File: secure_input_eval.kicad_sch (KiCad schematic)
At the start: 64 parts, among them CON1_STLINK1 ST-LINK, J10 masa pomiarowa, J18_CPU_CON1 Conn_CPU, J19 masa pomiarowa, J23 masa pomiarowa, J24 masa pomiarowa, J25 masa pomiarowa, J26 masa pomiarowa, J27_USART3 USART, J28_PIN14_PA7 TOUCH_SINGLE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

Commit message: TITLES&SUBTITLES POSITIONS & NAMES.
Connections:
- net SW5_TCH: now also J18_CPU_CON1.14 (Pin_14)
- net SW7_touch_single: no longer J18_CPU_CON1.14 (Pin_14)

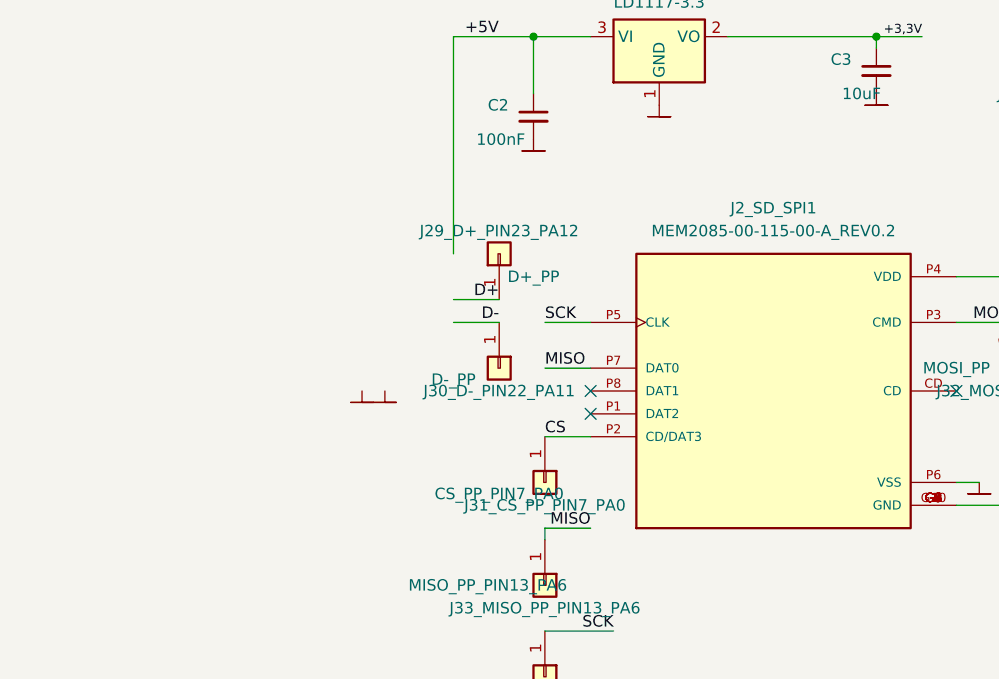
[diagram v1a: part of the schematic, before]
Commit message: symbole i footprinty #1
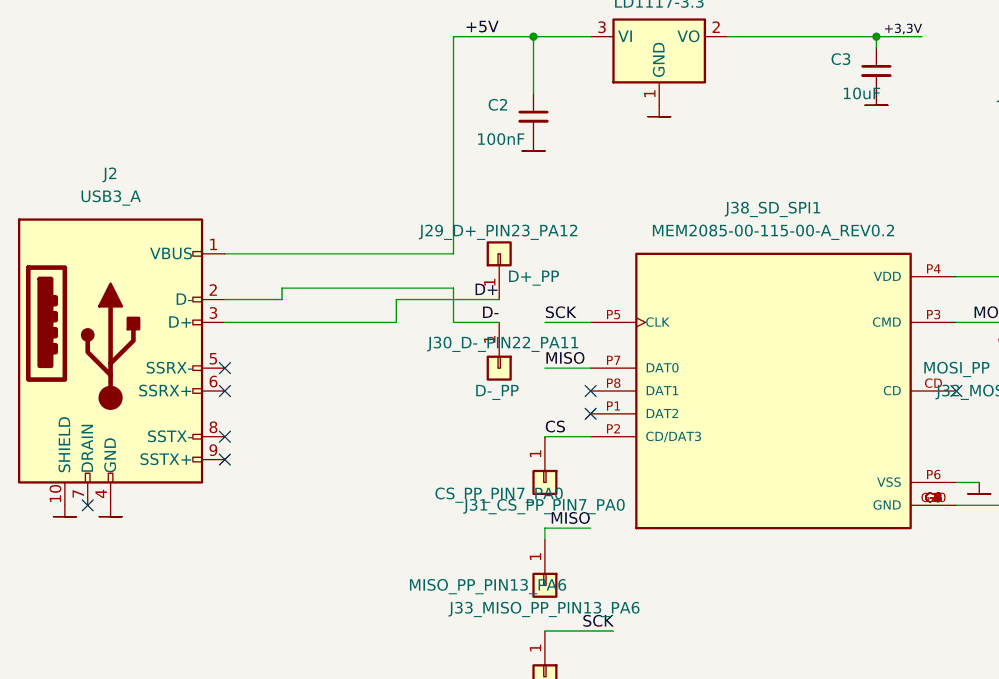
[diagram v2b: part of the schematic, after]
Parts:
- added J2: USB3_A, foots6:USB3_A_Amphenol_GSB316441CEU, symbol Connector:USB3_A
- H5: footprint secure_input_pen:MountingHole_2mm -> foots6:MountingHole_2mm
- renumbered J2_SD_SPI1 to J38_SD_SPI1
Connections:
- net +5V: now also J2.1 (VBUS)
- net D+: now also J2.3 (D+)
- net D-: now also J2.2 (D-)
- net masa: now also J2.10 (SHIELD), J2.4 (GND)
- no-connect marks 3 -> 8
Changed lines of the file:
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@@
 	)
 	(no_connect
+		(at -8.89 74.93)
+	)
+	(no_connect
 		(at 87.63 62.23)
 	)
 	(no_connect
+		(at 6.35 69.85)
+	)
+	(no_connect
+		(at 6.35 59.69)
+	)
+	(no_connect
+		(at 6.35 62.23)
+	)
+	(no_connect
 		(at 46.99 62.23)
 	)
 	(no_connect
+		(at 6.35 67.31)
+	)
+	(no_connect
 		(at 46.99 64.77)
 	)
 	(wire
 		(pts
+			(xy 12.7 52.07) (xy 6.35 52.07)
+		)
+		(stroke
+			(width 0)
+			(type default)
+		)
+	)
+	(wire
+		(pts
 			(xy 204.47 127) (xy 209.55 127)
 		)
@@
 	(wire
 		(pts
+			(xy 6.35 46.99) (xy 31.75 46.99)
+		)
+		(stroke
+			(width 0)
+			(type default)
+		)
+	)
+	(wire
+		(pts
 			(xy 262.89 130.302) (xy 270.002 130.302)
 		)
@@
 	(wire
 		(pts
+			(xy 31.75 50.8) (xy 12.7 50.8)
+		)
+		(stroke
+			(width 0)
+			(type default)
+		)
+	)
+	(wire
+		(pts
 			(xy 156.972 111.76) (xy 168.91 111.76)
 		)
@@
 	(wire
 		(pts
+			(xy 25.4 52.07) (xy 36.83 52.07)
+		)
+		(stroke
+			(width 0)
+			(type default)
+		)
+	)
+	(wire
+		(pts
 			(xy 140.97 52.07) (xy 149.86 52.07)
 		)
@@
 	(wire
 		(pts
-			(xy 163.83 129.54) (xy 168.91 129.54)
+			(xy 12.7 50.8) (xy 12.7 52.07)
 		)
 		(stroke
@@
 	(wire
 		(pts
-			(xy 241.3 139.7) (xy 247.65 139.7)
+			(xy 163.83 129.54) (xy 168.91 129.54)
 		)
 		(stroke
@@
 	(wire
 		(pts
-			(xy 118.11 95.25) (xy 113.03 95.25)
+			(xy 241.3 139.7) (xy 247.65 139.7)
 		)
 		(stroke
@@
 	(wire
 		(pts
-			(xy 31.75 52.07) (xy 36.83 52.07)
+			(xy 118.11 95.25) (xy 113.03 95.25)
 		)
 		(stroke
@@
 	(wire
 		(pts
+			(xy 31.75 54.61) (xy 31.75 50.8)
+		)
+		(stroke
+			(width 0)
+			(type default)
+		)
+	)
+	(wire
+		(pts
 			(xy 161.29 41.91) (xy 163.83 41.91)
 		)
@@
 	(wire
 		(pts
+			(xy 6.35 54.61) (xy 25.4 54.61)
+		)
+		(stroke
+			(width 0)
+			(type default)
+		)
+	)
+	(wire
+		(pts
 			(xy 204.47 124.46) (xy 209.55 124.46)
 		)
@@
 	(wire
 		(pts
+			(xy 25.4 54.61) (xy 25.4 52.07)
+		)
+		(stroke
+			(width 0)
+			(type default)
+		)
+	)
+	(wire
+		(pts
 			(xy 87.63 54.61) (xy 93.98 54.61)
 		)
@@
 			)
 		)
-		(property "Footprint" "secure_input_pen:MountingHole_2mm"
+		(property "Footprint" "foots6:MountingHole_2mm"
 			(at 208.28 17.78 0)
 			(effects
@@
 		(dnp no)
 		(fields_autoplaced yes)
-		(property "Reference" "J2_SD_SPI1"
+		(property "Reference" "J38_SD_SPI1"
 			(at 67.31 41.91 0)
 			(effects
@@
 			(project ""
 				(path "/df5b5a44-5c39-424a-a3aa-4eb40edf4ed4"
-					(reference "J2_SD_SPI1")
+					(reference "J38_SD_SPI1")
 					(unit 1)
 				)
@@
 	(symbol
 		(lib_id "sp3jdz:masa")
-		(at 24.13 62.23 0)
+		(at -11.43 74.93 0)
 		(unit 1)
 		(exclude_from_sim no)
@@
 		(fields_autoplaced yes)
 		(property "Reference" "#PWR04"
-			(at 24.13 68.58 0)
+			(at -11.43 81.28 0)
 			(effects
 				(font
@@
 		)
 		(property "Value" "masa"
-			(at 24.13 64.77 0)
+			(at -11.43 77.47 0)
 			(effects
 				(font
@@
 		)
 		(property "Footprint" ""
-			(at 24.13 62.23 0)
+			(at -11.43 74.93 0)
 			(effects
 				(font
@@
 		)
 		(property "Datasheet" ""
-			(at 24.13 62.23 0)
+			(at -11.43 74.93 0)
 			(effects
 				(font
@@
 		)
 		(property "Description" ""
-			(at 24.13 62.23 0)
+			(at -11.43 74.93 0)
 			(effects
 				(font
@@
 	)
 	(symbol
+		(lib_id "Connector:USB3_A")
+		(at -6.35 57.15 0)
+		(unit 1)
+		(exclude_from_sim no)
+		(in_bom yes)
+		(on_board yes)
+		(dnp no)
+		(fields_autoplaced yes)
+		(property "Reference" "J2"
+			(at -6.35 38.1 0)
+			(effects
+				(font
+					(size 1.27 1.27)
+				)
+			)
+		)
+		(property "Value" "USB3_A"
+			(at -6.35 40.64 0)
+			(effects
+				(font
+					(size 1.27 1.27)
+				)
+			)
+		)
+		(property "Footprint" "foots6:USB3_A_Amphenol_GSB316441CEU"
+			(at -2.54 54.61 0)
+			(effects
+				(font
+					(size 1.27 1.27)
+				)
+				(hide yes)
+			)
+		)
+		(property "Datasheet" "~"
+			(at -2.54 54.61 0)
+			(effects
+				(font
+					(size 1.27 1.27)
+				)
+				(hide yes)
+			)
+		)
+		(property "Description" "USB 3.0 A connector"
+			(at -6.35 57.15 0)
+			(effects
+				(font
+					(size 1.27 1.27)
+				)
+				(hide yes)
+			)
+		)
+		(pin "1"
+		)
+		(pin "10"
+		)
+		(pin "7"
+		)
+		(pin "4"
+		)
+		(pin "3"
+		)
+		(pin "6"
+		)
+		(pin "5"
+		)
+		(pin "9"
+		)
+		(pin "2"
+		)
+		(pin "8"
+		)
+		(instances
+			(project ""
+				(path "/df5b5a44-5c39-424a-a3aa-4eb40edf4ed4"
+					(reference "J2")
+					(unit 1)
+				)
+			)
+		)
+	)
+	(symbol
 		(lib_id "sp3jdz:masa")
 		(at 283.21 147.32 0)
@@
 		(dnp no)
 		(property "Reference" "J30_D-_PIN22_PA11"
-			(at 36.83 62.23 90)
+			(at 37.338 56.896 90)
 			(effects
 				(font
@@
 		)
 		(property "Value" "D-_PP"
-			(at 31.75 60.96 90)
+			(at 36.576 62.23 90)
 			(effects
 				(font
@@
 	(symbol
 		(lib_id "sp3jdz:masa")
-		(at 21.59 62.23 0)
+		(at -6.35 74.93 0)
 		(unit 1)
 		(exclude_from_sim no)
@@
 		(fields_autoplaced yes)
 		(property "Reference" "#PWR05"
-			(at 21.59 68.58 0)
+			(at -6.35 81.28 0)
 			(effects
 				(font
@@
 		)
 		(property "Value" "masa"
-			(at 21.59 64.77 0)
+			(at -6.35 77.47 0)
 			(effects
 				(font
@@
 		)
 		(property "Footprint" ""
-			(at 21.59 62.23 0)
+			(at -6.35 74.93 0)
 			(effects
 				(font
@@
 		)
 		(property "Datasheet" ""
-			(at 21.59 62.23 0)
+			(at -6.35 74.93 0)
 			(effects
 				(font
@@
 		)
 		(property "Description" ""
-			(at 21.59 62.23 0)
+			(at -6.35 74.93 0)
 			(effects
 				(font
